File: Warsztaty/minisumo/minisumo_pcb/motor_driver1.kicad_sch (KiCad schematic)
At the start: 5 parts, among them U2 TB6612FNG

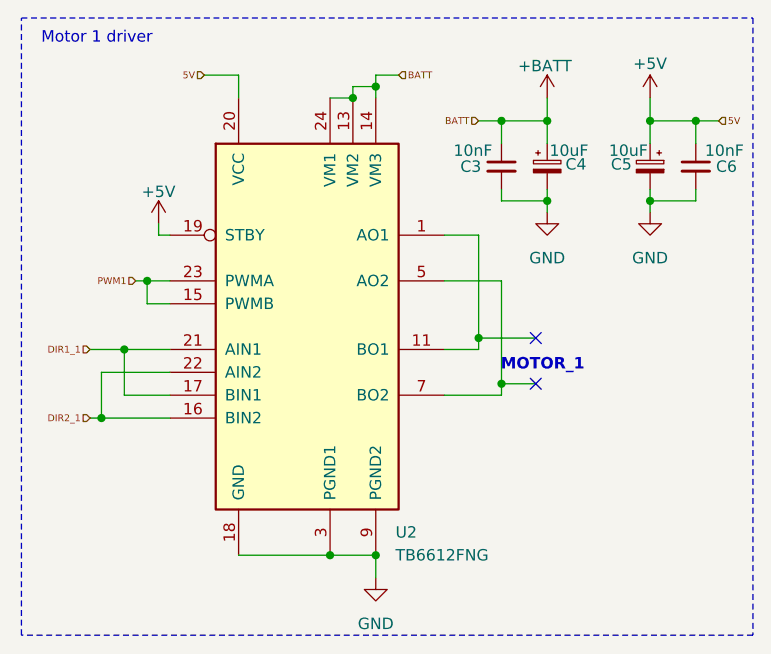
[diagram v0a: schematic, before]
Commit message: laczenie hierarchiczne schematu
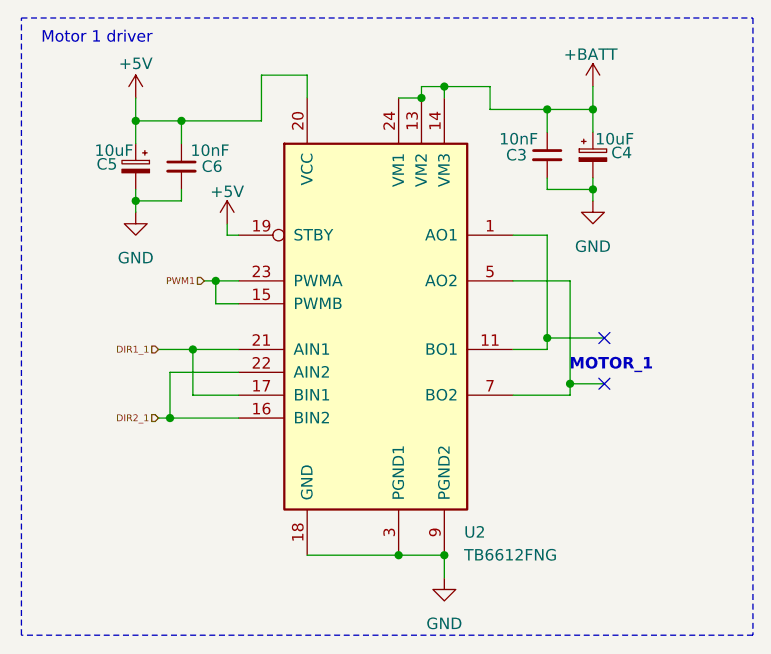
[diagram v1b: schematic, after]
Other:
- moved on the sheet: C3, C4, C5, C6, U2

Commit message: wstepnie skonczony schemat
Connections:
- net DIR1_1 renamed DIR1
- net DIR2_1 renamed DIR2
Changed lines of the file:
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@@
 		)
 	)
-	(hierarchical_label "DIR1_1"
+	(hierarchical_label "DIR1"
 		(shape input)
 		(at 29.21 50.8 180)
@@
 		)
 	)
-	(hierarchical_label "DIR2_1"
+	(hierarchical_label "DIR2"
 		(shape input)
 		(at 29.21 58.42 180)
@@
 					(unit 1)
 				)
+				(path "/7b99a4ad-c15f-48f5-acdf-b2b295c8ee3b/6370311e-bb6b-4c97-a800-647b77b0b74c"
+					(reference "#PWR044")
+					(unit 1)
+				)
 			)
 		)
@@
 					(unit 1)
 				)
+				(path "/7b99a4ad-c15f-48f5-acdf-b2b295c8ee3b/6370311e-bb6b-4c97-a800-647b77b0b74c"
+					(reference "U13")
+					(unit 1)
+				)
 			)
 		)
@@
 				(path "/7b99a4ad-c15f-48f5-acdf-b2b295c8ee3b/6ae141c6-db4a-4bb1-a0f3-35ba0e4d6945"
 					(reference "#PWR01")
+					(unit 1)
+				)
+				(path "/7b99a4ad-c15f-48f5-acdf-b2b295c8ee3b/6370311e-bb6b-4c97-a800-647b77b0b74c"
+					(reference "#PWR042")
 					(unit 1)
 				)
@@
 					(unit 1)
 				)
+				(path "/7b99a4ad-c15f-48f5-acdf-b2b295c8ee3b/6370311e-bb6b-4c97-a800-647b77b0b74c"
+					(reference "#PWR043")
+					(unit 1)
+				)
 			)
 		)
@@
 					(unit 1)
 				)
+				(path "/7b99a4ad-c15f-48f5-acdf-b2b295c8ee3b/6370311e-bb6b-4c97-a800-647b77b0b74c"
+					(reference "C19")
+					(unit 1)
+				)
 			)
 		)
@@
 					(unit 1)
 				)
+				(path "/7b99a4ad-c15f-48f5-acdf-b2b295c8ee3b/6370311e-bb6b-4c97-a800-647b77b0b74c"
+					(reference "C18")
+					(unit 1)
+				)
 			)
 		)
@@
 				(path "/7b99a4ad-c15f-48f5-acdf-b2b295c8ee3b/6ae141c6-db4a-4bb1-a0f3-35ba0e4d6945"
 					(reference "#PWR012")
+					(unit 1)
+				)
+				(path "/7b99a4ad-c15f-48f5-acdf-b2b295c8ee3b/6370311e-bb6b-4c97-a800-647b77b0b74c"
+					(reference "#PWR040")
 					(unit 1)
 				)
@@
 					(unit 1)
 				)
+				(path "/7b99a4ad-c15f-48f5-acdf-b2b295c8ee3b/6370311e-bb6b-4c97-a800-647b77b0b74c"
+					(reference "#PWR041")
+					(unit 1)
+				)
 			)
 		)
@@
 				(path "/7b99a4ad-c15f-48f5-acdf-b2b295c8ee3b/6ae141c6-db4a-4bb1-a0f3-35ba0e4d6945"
 					(reference "C3")
+					(unit 1)
+				)
+				(path "/7b99a4ad-c15f-48f5-acdf-b2b295c8ee3b/6370311e-bb6b-4c97-a800-647b77b0b74c"
+					(reference "C20")
 					(unit 1)
 				)
@@
 					(unit 1)
 				)
+				(path "/7b99a4ad-c15f-48f5-acdf-b2b295c8ee3b/6370311e-bb6b-4c97-a800-647b77b0b74c"
+					(reference "#PWR051")
+					(unit 1)
+				)
 			)
 		)
@@
 					(unit 1)
 				)
+				(path "/7b99a4ad-c15f-48f5-acdf-b2b295c8ee3b/6370311e-bb6b-4c97-a800-647b77b0b74c"
+					(reference "C23")
+					(unit 1)
+				)

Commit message: chyba gotowy schemat
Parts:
- C3, C4, C5, C6: footprint (none) -> Capacitor_SMD:C_0805_2012Metric_Pad1.18x1.45mm_HandSolder
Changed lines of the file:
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@@
 			)
 		)
-		(property "Footprint" ""
+		(property "Footprint" "Capacitor_SMD:C_0805_2012Metric_Pad1.18x1.45mm_HandSolder"
 			(at 31.75 30.48 0)
 			(effects
@@
 			)
 		)
-		(property "Footprint" ""
+		(property "Footprint" "Capacitor_SMD:C_0805_2012Metric_Pad1.18x1.45mm_HandSolder"
 			(at 26.67 30.48 0)
 			(effects
@@
 			)
 		)
-		(property "Footprint" ""
+		(property "Footprint" "Capacitor_SMD:C_0805_2012Metric_Pad1.18x1.45mm_HandSolder"
 			(at 72.39 29.21 0)
 			(effects
@@
 			)
 		)
-		(property "Footprint" ""
+		(property "Footprint" "Capacitor_SMD:C_0805_2012Metric_Pad1.18x1.45mm_HandSolder"
 			(at 77.47 29.21 0)
 			(effects
